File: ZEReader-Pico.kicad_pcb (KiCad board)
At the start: 2 copper layers, 100 x 120 mm, 19 parts, among them J1 Micro_SD_Card_Det2, J2 Conn_01x03_Pin, J3 Conn_01x03_Pin, SW1 SW_Push, SW2 SW_Push, SW3 SW_Push, U1 Pico

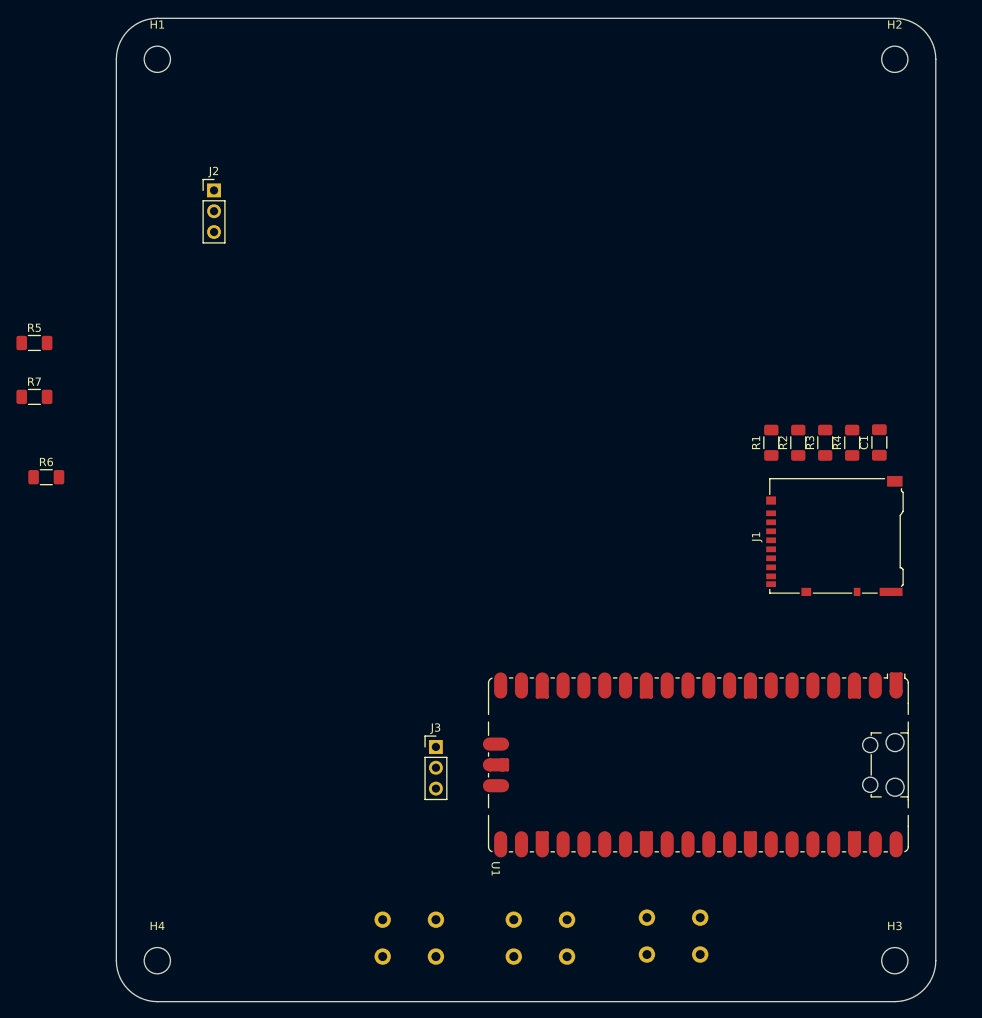
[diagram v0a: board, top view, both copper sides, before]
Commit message: Add EPD Driver Circuit
Signed-off-by: Anna-Lena Marx <anna-lena.marx@web.de>
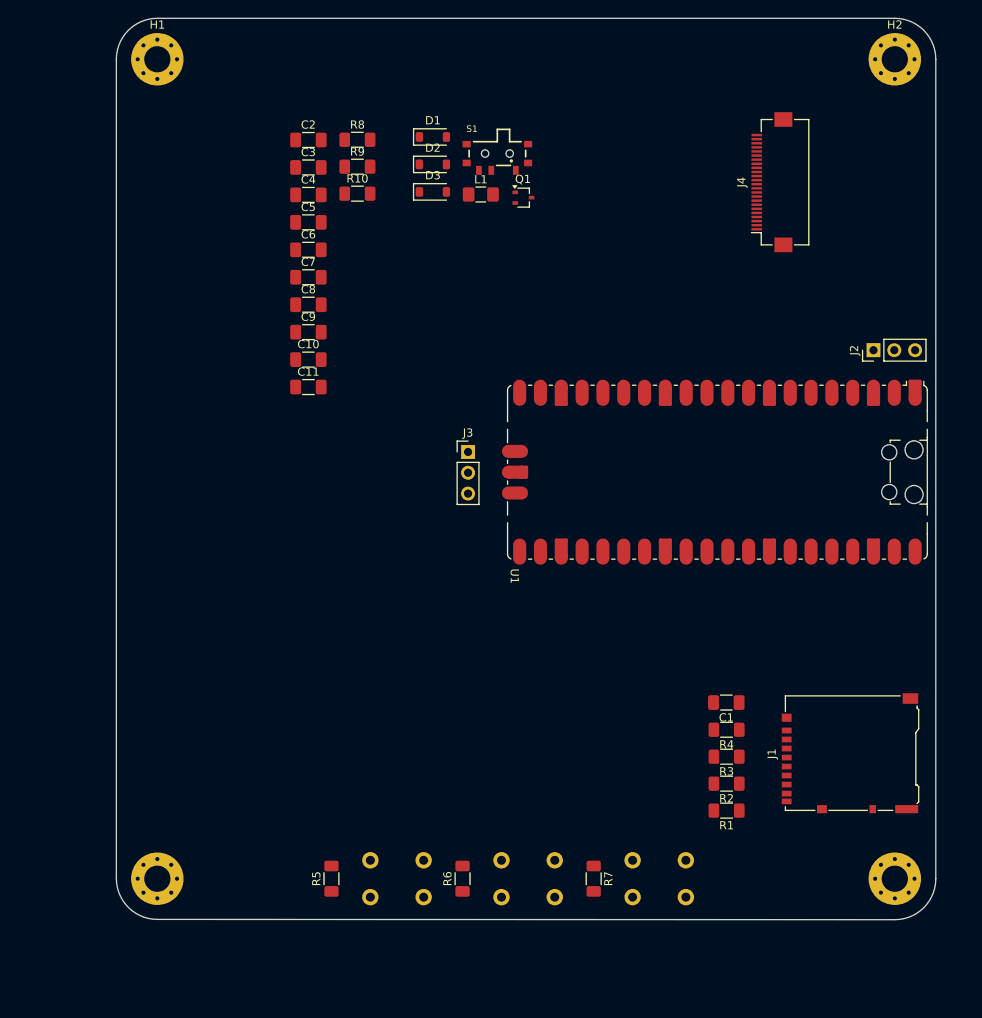
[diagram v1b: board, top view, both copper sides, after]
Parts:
- added C10: 1uF, Capacitor_SMD:C_1206_3216Metric_Pad1.33x1.80mm_HandSolder, F.Cu at (73.4, 66.7)
- added C11: 1uF, Capacitor_SMD:C_1206_3216Metric_Pad1.33x1.80mm_HandSolder, F.Cu at (73.4, 70.0)
- added C2: 4.7uF, Capacitor_SMD:C_1206_3216Metric_Pad1.33x1.80mm_HandSolder, F.Cu at (73.4, 39.9)
- added C3: 4.7uF, Capacitor_SMD:C_1206_3216Metric_Pad1.33x1.80mm_HandSolder, F.Cu at (73.4, 43.2)
- added C4: 1uF, Capacitor_SMD:C_1206_3216Metric_Pad1.33x1.80mm_HandSolder, F.Cu at (73.4, 46.5)
- added C5: 1uF, Capacitor_SMD:C_1206_3216Metric_Pad1.33x1.80mm_HandSolder, F.Cu at (73.4, 49.9)
- added C6: 1uF, Capacitor_SMD:C_1206_3216Metric_Pad1.33x1.80mm_HandSolder, F.Cu at (73.4, 53.2)
- added C7: 1uF, Capacitor_SMD:C_1206_3216Metric_Pad1.33x1.80mm_HandSolder, F.Cu at (73.4, 56.6)
- added C8: 1uF, Capacitor_SMD:C_1206_3216Metric_Pad1.33x1.80mm_HandSolder, F.Cu at (73.4, 60.0)
- added C9: 1uF, Capacitor_SMD:C_1206_3216Metric_Pad1.33x1.80mm_HandSolder, F.Cu at (73.4, 63.3)
- added D1: MBR0530, Diode_SMD:D_SOD-123, F.Cu at (88.6, 39.5)
- added D2: MBR0530, Diode_SMD:D_SOD-123, F.Cu at (88.6, 42.8)
- added D3: MBR0530, Diode_SMD:D_SOD-123, F.Cu at (88.6, 46.2)
- added J4: Conn_01x24_MountingPin, Connector_FFC-FPC:Hirose_FH12-24S-0.5SH_1x24-1MP_P0.50mm_Horizontal, F.Cu at (130.0, 45.0)
- added L1: 10uH 1A, Inductor_SMD:L_1206_3216Metric_Pad1.42x1.75mm_HandSolder, F.Cu at (94.5, 46.5)
- added Q1: Si1308EDL, Package_TO_SOT_SMD:SOT-323_SC-70, F.Cu at (99.7, 46.9)
- added R10: 3, Resistor_SMD:R_1206_3216Metric_Pad1.30x1.75mm_HandSolder, F.Cu at (79.4, 46.4)
- added R8: 10k, Resistor_SMD:R_1206_3216Metric_Pad1.30x1.75mm_HandSolder, F.Cu at (79.4, 39.8)
- added R9: 0.47, Resistor_SMD:R_1206_3216Metric_Pad1.30x1.75mm_HandSolder, F.Cu at (79.4, 43.1)
- added S1: 450404015514, 4504040015514:450404015514, F.Cu at (96.5, 41.5)
- H1, H2, H3, H4: footprint MountingHole:MountingHole_3.2mm_M3 -> MountingHole:MountingHole_3.2mm_M3_Pad_Via
- U1: footprint Module:RaspberryPi_Pico_SMD_HandSolder -> Module:RaspberryPi_Pico_SMD_HandSolder_Anna
- moved R7 90.1 mm to (108.2, 130.0), turned to -90 degrees
- moved J2 82.8 mm to (142.4, 65.5), turned to 90 degrees
- moved R5 74.8 mm to (76.2, 130.0), turned to 90 degrees
- moved R6 70.6 mm to (92.2, 130.0), turned to 90 degrees
- moved R1 45.2 mm to (124.5, 121.7), turned to 180 degrees
- moved R2 42.5 mm to (124.5, 118.4), turned to 180 degrees
- moved R3 40.2 mm to (124.5, 115.1), turned to 180 degrees
- moved R4 38.2 mm to (124.5, 111.8), turned to 180 degrees
- moved C1 36.8 mm to (124.4, 108.5), turned to 180 degrees
- moved J3 36.2 mm to (92.9, 77.9)
- moved U1 35.8 mm to (123.3, 80.4)
- moved J1 26.6 mm to (139.5, 114.7)
- moved H3 10.0 mm to (145.0, 130.0)
- moved H4 10.0 mm to (55.0, 130.0)
- moved SW1 7.40 mm to (87.5, 127.8)
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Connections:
- J2 pad 1: Net-(J2-Pin_1) -> GND
- J3 pad 2: Net-(J3-Pin_2) -> GND
- R1 pad 1: +3.3V -> Net-(J1-VDD)
- R2 pad 1: +3.3V -> Net-(J1-VDD)
- R3 pad 1: +3.3V -> Net-(J1-VDD)
- R4 pad 1: +3.3V -> Net-(J1-VDD)
- U1 pad 1: Net-(J2-Pin_1) -> Net-(J2-Pin_3)
- U1 pad 10: unconnected-(U1-GPIO7-Pad10) -> EPD_BUSY
- U1 pad 11: unconnected-(U1-GPIO8-Pad11) -> EPD_RST
- U1 pad 12: unconnected-(U1-GPIO9-Pad12) -> EPD_DC
- U1 pad 13: unconnected-(U1-GND-Pad13) -> GND
- U1 pad 14: SD_CLK-SCLK -> EPD_SCK
- U1 pad 15: SD_CMD-DI -> EPD_DIN
- U1 pad 16: SD_DAT0-DO -> unconnected-(U1-GPIO12-Pad16)
- U1 pad 17: SD_DAT3-CD-CS -> EPD_CS
- U1 pad 18: unconnected-(U1-GND-Pad18) -> GND
- U1 pad 21: unconnected-(U1-GPIO16-Pad21) -> SD_DAT0-DO
- U1 pad 22: unconnected-(U1-GPIO17-Pad22) -> SD_DAT3-CD-CS
- U1 pad 23: unconnected-(U1-GND-Pad23) -> GND
- U1 pad 24: unconnected-(U1-GPIO18-Pad24) -> SD_CLK-SCLK
- U1 pad 25: unconnected-(U1-GPIO19-Pad25) -> SD_CMD-DI
- U1 pad 28: unconnected-(U1-GND-Pad28) -> GND
- U1 pad 29: unconnected-(U1-GPIO22-Pad29) -> BTN_1
- U1 pad 3: Net-(J2-Pin_3) -> GND
- U1 pad 31: unconnected-(U1-GPIO26_ADC0-Pad31) -> BTN_2
- U1 pad 32: unconnected-(U1-GPIO27_ADC1-Pad32) -> BTN_3
- U1 pad 33: unconnected-(U1-AGND-Pad33) -> GND
- U1 pad 38: unconnected-(U1-GND-Pad38) -> GND
- U1 pad 4: BTN_1 -> unconnected-(U1-GPIO2-Pad4)
- U1 pad 5: BTN_2 -> unconnected-(U1-GPIO3-Pad5)
- U1 pad 6: BTN_3 -> unconnected-(U1-GPIO4-Pad6)
- U1 pad 8: unconnected-(U1-GND-Pad8) -> GND
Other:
- board size 100 x 120 mm -> 100 x 110 mm

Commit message: Added USB-C, Battery Charging andOn/Off
Signed-off-by: Anna-Lena Marx <anna-lena.marx@web.de>
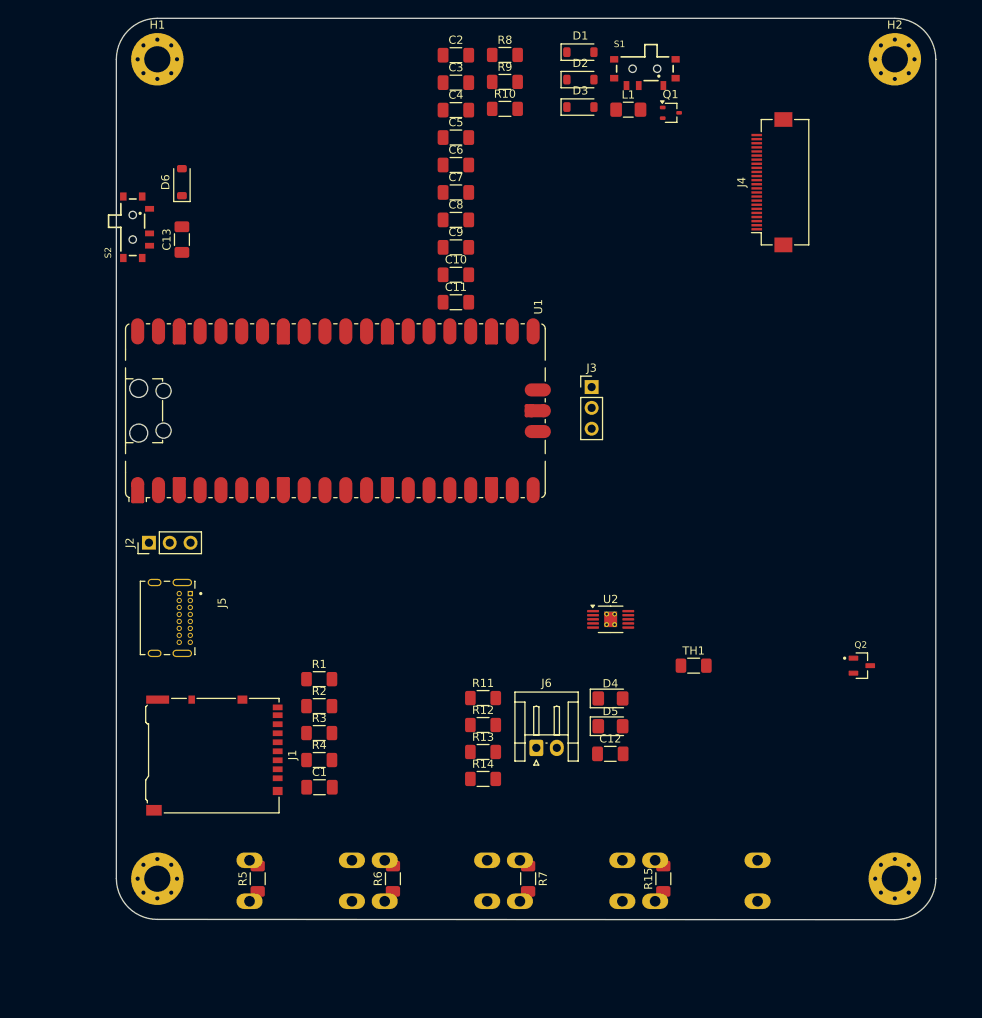
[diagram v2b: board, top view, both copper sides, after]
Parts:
- added C12: 10uF, Capacitor_SMD:C_1206_3216Metric_Pad1.33x1.80mm_HandSolder, F.Cu at (110.3, 114.8)
- added C13: 10uF, Capacitor_SMD:C_1206_3216Metric_Pad1.33x1.80mm_HandSolder, F.Cu at (58.0, 52.0)
- added D4: LED, LED_SMD:LED_1206_3216Metric_Pad1.42x1.75mm_HandSolder, F.Cu at (110.3, 108.0)
- added D5: LED, LED_SMD:LED_1206_3216Metric_Pad1.42x1.75mm_HandSolder, F.Cu at (110.3, 111.4)
- added D6: MBR0530, Diode_SMD:D_SOD-123, F.Cu at (58.0, 45.0)
- added J5: UJ20-C-H-G-SMT-TR, UJ20:CUI_UJ20-C-H-G-SMT-TR, F.Cu at (55.0, 98.2)
- added J6: Conn_01x02_Socket, Connector_JST:JST_EH_S2B-EH_1x02_P2.50mm_Horizontal, F.Cu at (101.2, 114.0)
- added Q2: DMG2305UX-7, Package_TO_SOT_SMD:SOT91P240X110-3N_DMG2305UX-7, F.Cu at (141.0, 104.0)
- added R11: 2.7k, Resistor_SMD:R_1206_3216Metric_Pad1.30x1.75mm_HandSolder, F.Cu at (94.8, 108.0)
- added R12: 2k, Resistor_SMD:R_1206_3216Metric_Pad1.30x1.75mm_HandSolder, F.Cu at (94.8, 111.2)
- added R13: 1.5k, Resistor_SMD:R_1206_3216Metric_Pad1.30x1.75mm_HandSolder, F.Cu at (94.8, 114.5)
- added R14: 1.5k, Resistor_SMD:R_1206_3216Metric_Pad1.30x1.75mm_HandSolder, F.Cu at (94.8, 117.8)
- added R15: 4.7k, Resistor_SMD:R_1206_3216Metric_Pad1.30x1.75mm_HandSolder, F.Cu at (116.8, 130.0)
- added S2: 450404015514, 4504040015514:450404015514, F.Cu at (52.0, 50.5)
- added SW4: SW_Push, Button_Switch_THT:SW_PUSH-12mm, B.Cu at (128.2, 127.8)
- added TH1: Thermistor_NTC 10k, Resistor_SMD:R_1206_3216Metric_Pad1.30x1.75mm_HandSolder, F.Cu at (120.5, 104.0)
- added U2: BQ24090DGQ, Package_SO:HVSSOP-10-1EP_3x3mm_P0.5mm_EP1.57x1.88mm_ThermalVias, F.Cu at (110.3, 98.3)
- C1: value 22u -> 10uF
- SW1, SW2, SW3: footprint Button_Switch_THT:SW_PUSH_6mm_H4.3mm -> Button_Switch_THT:SW_PUSH-12mm
- moved J2 91.5 mm to (54.0, 89.0)
- moved J1 77.6 mm to (62.0, 115.0), turned to -90 degrees
- moved R1 52.2 mm to (74.8, 105.6), turned to 0 degrees
- moved C1 50.7 mm to (74.8, 118.8), turned to 0 degrees
- moved R2 50.6 mm to (74.8, 108.9), turned to 0 degrees
- moved R4 49.8 mm to (74.8, 115.5), turned to 0 degrees
- moved R3 49.8 mm to (74.8, 112.2), turned to 0 degrees
- moved U1 47.2 mm to (76.7, 72.9), turned to 90 degrees
- moved C10 20.8 mm to (91.4, 56.3)
- moved C11 20.8 mm to (91.4, 59.6)
- moved C2 20.8 mm to (91.4, 29.5)
- moved C3 20.8 mm to (91.4, 32.9)
- moved C4 20.8 mm to (91.4, 36.2)
- moved C5 20.8 mm to (91.4, 39.5)
- moved C6 20.8 mm to (91.4, 42.9)
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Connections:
- J2 pad 1: GND -> Net-(J2-Pin_1)
- J2 pad 3: Net-(J2-Pin_3) -> GND
- U1 pad 1: Net-(J2-Pin_3) -> Net-(J2-Pin_1)
- U1 pad 10: EPD_BUSY -> unconnected-(U1-GPIO7-Pad10)
- U1 pad 11: EPD_RST -> unconnected-(U1-GPIO8-Pad11)
- U1 pad 12: EPD_DC -> unconnected-(U1-GPIO9-Pad12)
- U1 pad 14: EPD_SCK -> SD_CLK-SCLK
- U1 pad 15: EPD_DIN -> SD_CMD-DI
- U1 pad 16: unconnected-(U1-GPIO12-Pad16) -> SD_DAT0-DO
- U1 pad 17: EPD_CS -> SD_DAT3-CD-CS
- U1 pad 21: SD_DAT0-DO -> unconnected-(U1-GPIO16-Pad21)
- U1 pad 22: SD_DAT3-CD-CS -> EPD_CS
- U1 pad 24: SD_CLK-SCLK -> EPD_SCK
- U1 pad 25: SD_CMD-DI -> EPD_DIN
- U1 pad 26: unconnected-(U1-GPIO20-Pad26) -> EPD_DC
- U1 pad 27: unconnected-(U1-GPIO21-Pad27) -> EPD_RST
- U1 pad 29: BTN_1 -> EPD_BUSY
- U1 pad 31: BTN_2 -> unconnected-(U1-GPIO26_ADC0-Pad31)
- U1 pad 32: BTN_3 -> unconnected-(U1-GPIO27_ADC1-Pad32)
- U1 pad 39: unconnected-(U1-VSYS-Pad39) -> VSYS
- U1 pad 4: unconnected-(U1-GPIO2-Pad4) -> BTN_1
- U1 pad 40: unconnected-(U1-VBUS-Pad40) -> VBUS
- U1 pad 41: Net-(J3-Pin_1) -> Net-(J3-Pin_3)
- U1 pad 43: Net-(J3-Pin_3) -> Net-(J3-Pin_1)
- U1 pad 5: unconnected-(U1-GPIO3-Pad5) -> BTN_2
- U1 pad 6: unconnected-(U1-GPIO4-Pad6) -> BTN_3
- U1 pad 7: unconnected-(U1-GPIO5-Pad7) -> BTN_4

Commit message: Added some more notes, testpoints and rechecked footprints and parts
Signed-off-by: Anna-Lena Marx <anna-lena.marx@web.de>
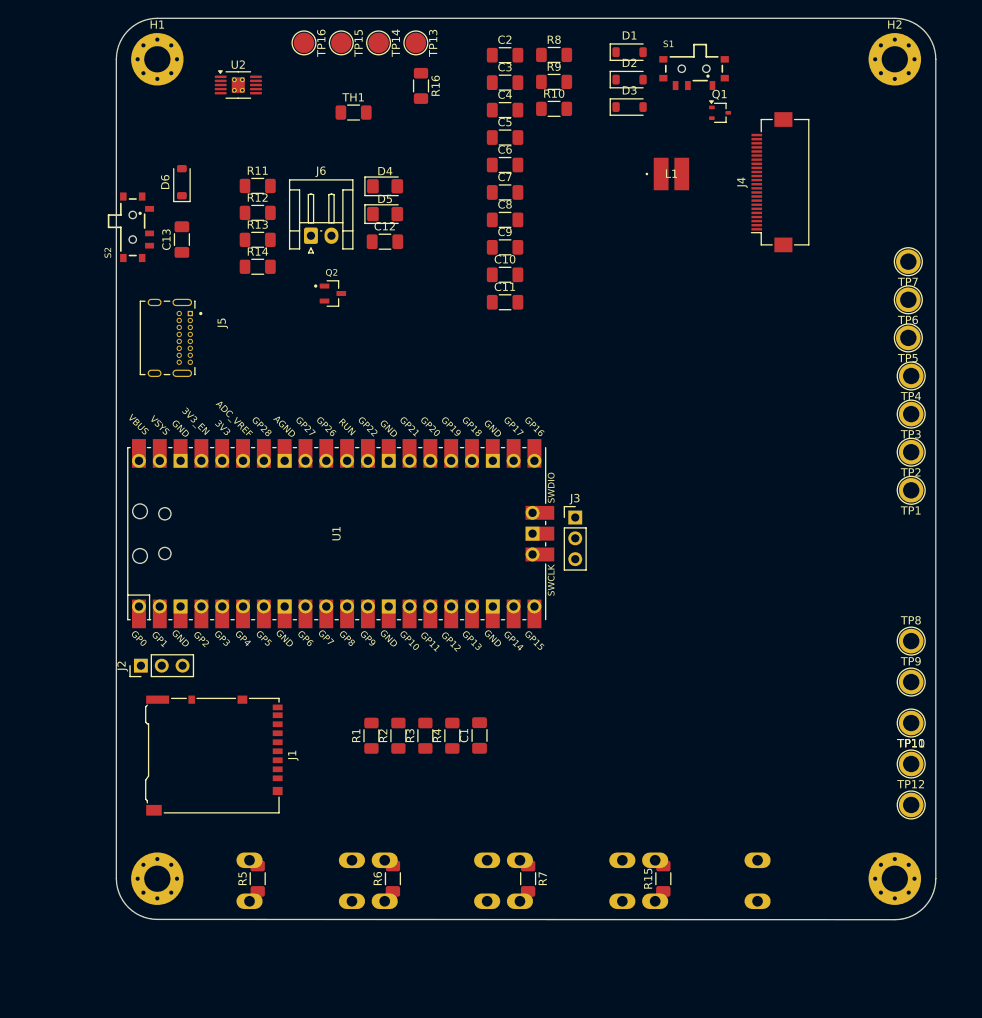
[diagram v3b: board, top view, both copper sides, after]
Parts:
- added R16: 0.5, Resistor_SMD:R_1206_3216Metric_Pad1.30x1.75mm_HandSolder, F.Cu at (87.2, 33.2)
- added TP1: EPD_BUSY, TestPoint:TestPoint_Plated_Hole_D2.0mm, F.Cu at (147.0, 82.6)
- added TP10: SD_DO, TestPoint:TestPoint_Plated_Hole_D2.0mm, F.Cu at (147.0, 111.0)
- added TP11: SD_SCLK, TestPoint:TestPoint_Plated_Hole_D2.0mm, F.Cu at (147.0, 116.0)
- added TP12: GND, TestPoint:TestPoint_Plated_Hole_D2.0mm, F.Cu at (147.0, 121.0)
- added TP13: USB_VBUS, TestPoint:TestPoint_Pad_D2.5mm, F.Cu at (86.5, 28.0)
- added TP14: V_USB_LIPO, TestPoint:TestPoint_Pad_D2.5mm, F.Cu at (82.0, 28.0)
- added TP15: VSYS, TestPoint:TestPoint_Pad_D2.5mm, F.Cu at (77.5, 28.0)
- added TP16: GND, TestPoint:TestPoint_Pad_D2.5mm, F.Cu at (72.9, 28.0)
- added TP2: EPD_RST, TestPoint:TestPoint_Plated_Hole_D2.0mm, F.Cu at (147.0, 78.0)
- added TP3: EPD_DC, TestPoint:TestPoint_Plated_Hole_D2.0mm, F.Cu at (147.0, 73.3)
- added TP4: EPD_CS, TestPoint:TestPoint_Plated_Hole_D2.0mm, F.Cu at (147.0, 68.7)
- added TP5: EPD_SCK, TestPoint:TestPoint_Plated_Hole_D2.0mm, F.Cu at (146.7, 64.0)
- added TP6: EPD_DIN, TestPoint:TestPoint_Plated_Hole_D2.0mm, F.Cu at (146.7, 59.4)
- added TP7: GND, TestPoint:TestPoint_Plated_Hole_D2.0mm, F.Cu at (146.7, 54.7)
- added TP8: SD_CS, TestPoint:TestPoint_Plated_Hole_D2.0mm, F.Cu at (147.0, 101.0)
- added TP9: SD_DI, TestPoint:TestPoint_Plated_Hole_D2.0mm, F.Cu at (147.0, 106.0)
- J2: value Conn_01x03_Pin -> UART
- J3: value Conn_01x03_Pin -> SWD
- L1: value 10uH 1A -> 10uH; footprint Inductor_SMD:L_1206_3216Metric_Pad1.42x1.75mm_HandSolder -> footprints:IND_IFSC_1515AH_VIS-L
- U1: footprint Module:RaspberryPi_Pico_SMD_HandSolder_Anna -> RPi_Pico:RPi_Pico_SMD_TH
- moved U2 79.5 mm to (64.9, 33.1)
- moved TH1 79.2 mm to (79.0, 36.5)
- moved Q2 78.9 mm to (76.4, 58.6)
- moved C12 68.3 mm to (82.8, 52.3)
- moved D4 68.3 mm to (82.8, 45.5)
- moved D5 68.3 mm to (82.8, 48.9)
- moved J6 68.3 mm to (73.8, 51.5)
- moved R11 68.3 mm to (67.2, 45.5)
- moved R12 68.3 mm to (67.2, 48.7)
- moved R13 68.3 mm to (67.2, 52.0)
- moved R14 68.3 mm to (67.2, 55.3)
- moved J5 34.2 mm to (55.0, 64.0)
- moved C1 20.5 mm to (94.3, 112.5), turned to 90 degrees
- moved R4 16.5 mm to (91.0, 112.5), turned to 90 degrees
- moved J3 16.0 mm to (106.0, 85.9)
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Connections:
- S2 pad 2: VSYS -> Net-(R16-Pad1)
- U1 pad 36: unconnected-(U1-3V3-Pad36) -> +3.3V

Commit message: Changed buttons to smaller ones, updated some comments
Signed-off-by: Anna-Lena Marx <anna-lena.marx@web.de>
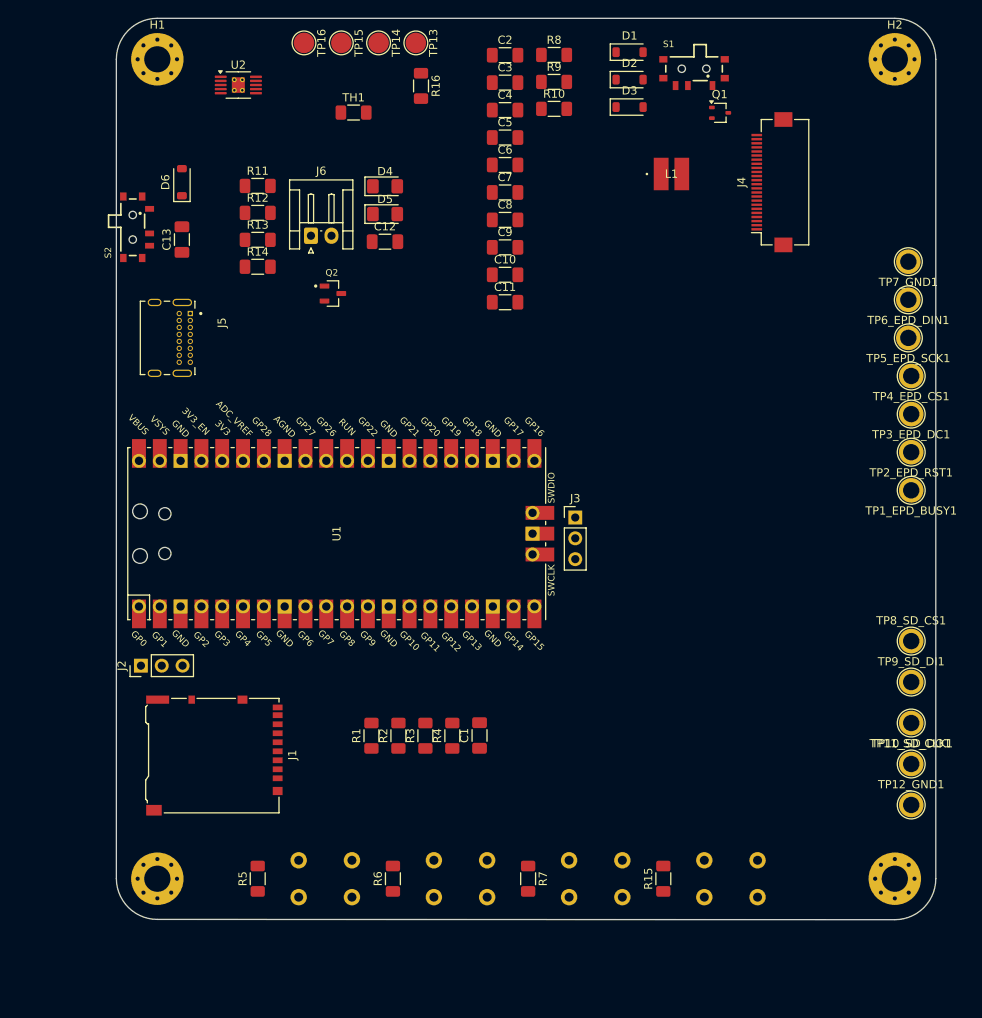
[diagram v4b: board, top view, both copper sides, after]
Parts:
- SW1, SW2, SW3, SW4: footprint Button_Switch_THT:SW_PUSH-12mm -> Button_Switch_THT:SW_PUSH_6mm
- renumbered TP10 to TP10_SD_DO1, TP11 to TP11_SD_CLK1, TP12 to TP12_GND1, TP1 to TP1_EPD_BUSY1, TP2 to TP2_EPD_RST1, TP3 to TP3_EPD_DC1, TP4 to TP4_EPD_CS1, TP5 to TP5_EPD_SCK1, TP6 to TP6_EPD_DIN1, TP7 to TP7_GND1, TP8 to TP8_SD_CS1, TP9 to TP9_SD_DI1
